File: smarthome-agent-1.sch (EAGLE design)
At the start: 9 parts, among them IC2 7808T, Q1 16Mhz, U1 ATMEGA328P_PDIP_EZ

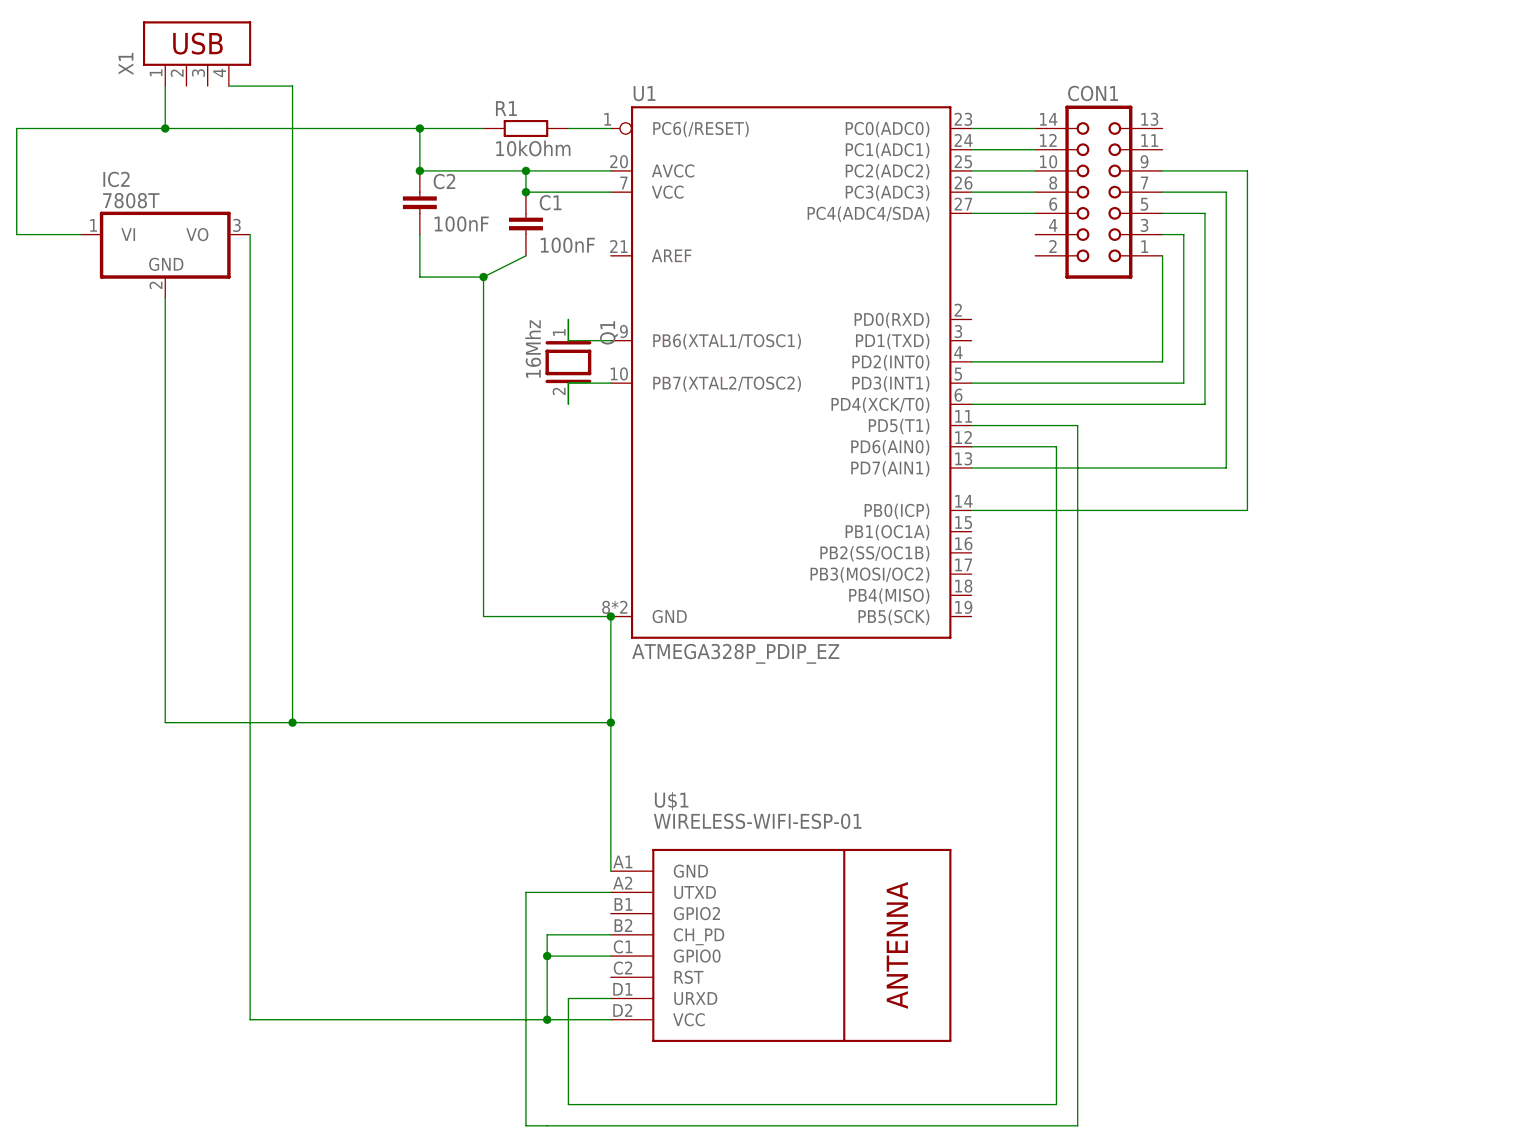
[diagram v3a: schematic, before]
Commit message: HOME-49 - Cleanup circuit and board design for production
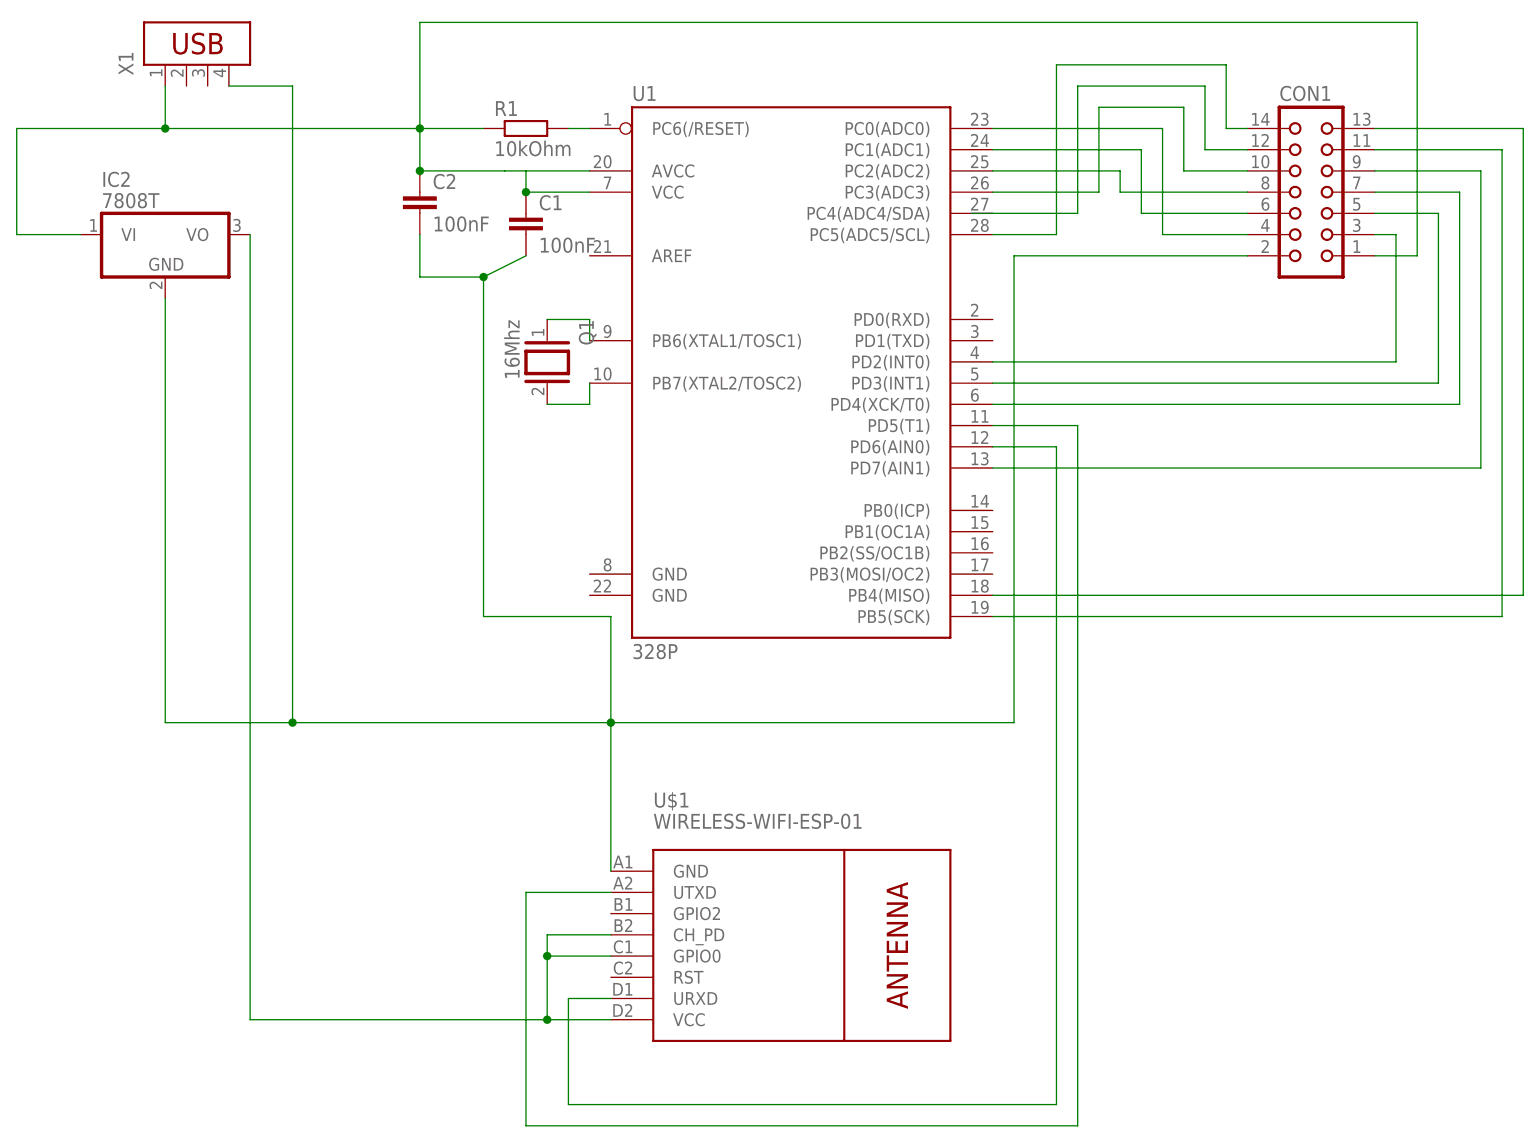
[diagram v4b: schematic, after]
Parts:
- U1: value ATMEGA328P_PDIP_EZ -> 328P; device SparkFun-IC-Microcontroller:ATMEGA328P_PDIP_EZ -> SparkFun-IC-Microcontroller:ATMEGA328P_PDIP
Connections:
- new net N$19: CON1.13, U1.PB4(MISO)
- new net N$20: CON1.14, U1.PC5(ADC5/SCL)
- net N$10: now also CON1.8, U1.PC2(ADC2); no longer CON1.7, U1.PD7(AIN1)
- net N$11: now also CON1.12, U1.PC4(ADC4/SDA); no longer CON1.14, U1.PC0(ADC0)
- net N$12: now also CON1.3, U1.PD2(INT0); no longer CON1.12, U1.PC1(ADC1)
- net N$13: now also CON1.5, U1.PD3(INT1); no longer CON1.10, U1.PC2(ADC2)
- net N$14: now also CON1.7, U1.PD4(XCK/T0); no longer CON1.8, U1.PC3(ADC3)
- net N$15: now also CON1.9, U1.PD7(AIN1); no longer CON1.6, U1.PC4(ADC4/SDA)
- net N$16: now also CON1.11, U1.PB5(SCK); no longer CON1.9, U1.PB0(ICP)
- net N$17: now also CON1.1
- net N$18: now also CON1.2; no longer U1.GND
- net N$7: now also CON1.10, U1.PC3(ADC3); no longer CON1.1, U1.PD2(INT0)
- net N$8: now also CON1.4, U1.PC0(ADC0); no longer CON1.3, U1.PD3(INT1)
- net N$9: now also CON1.6, U1.PC1(ADC1); no longer CON1.5, U1.PD4(XCK/T0)
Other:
- moved on the sheet: CON1, Q1
